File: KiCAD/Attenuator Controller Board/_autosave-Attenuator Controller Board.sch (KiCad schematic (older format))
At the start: 38 parts, among them J1 Barrel_Jack_Switch, J2 Conn_Coaxial, J3 Conn_Coaxial, J4 Conn_01x24_Female, J5 Conn_01x24_Female, J6 DSub9, J7 DSub9, J8 DSub9, J9 DSub_15_HD, U1 ADM3307EARUZ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

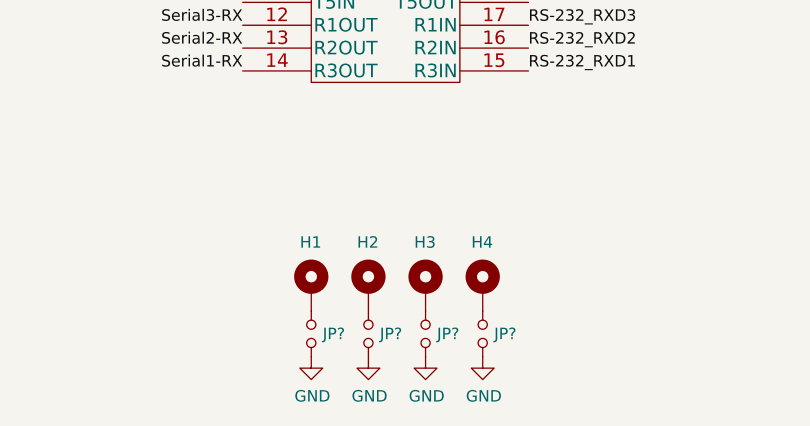
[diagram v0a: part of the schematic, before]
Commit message: Optional grounding of standoffs - ordered revision
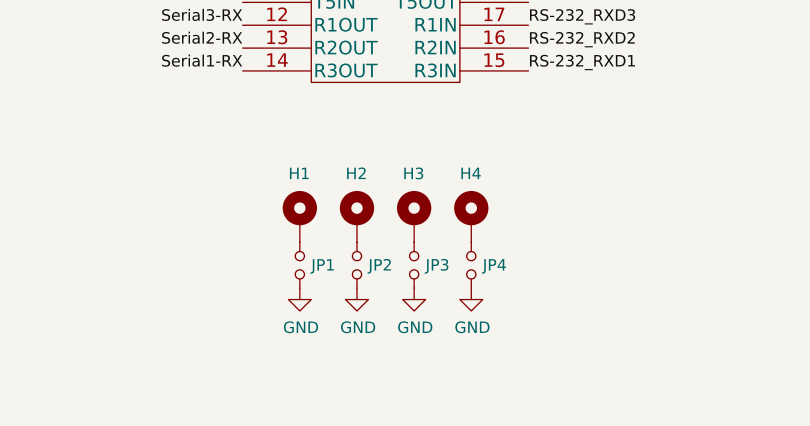
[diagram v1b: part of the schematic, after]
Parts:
- gave numbers to parts that had none: 4
- renumbered H3 to H1, H4 to H2, H1 to H3, H2 to H4
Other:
- moved on the sheet: H1, H2, H3, H4, JP1, JP2, JP3, JP4
